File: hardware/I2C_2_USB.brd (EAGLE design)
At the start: 14.9 x 20.3 mm, 13 parts, among them CN1 1X4-BIG, J3 USB-MICROB, U1 ATMEGA328P-MU-QFN32

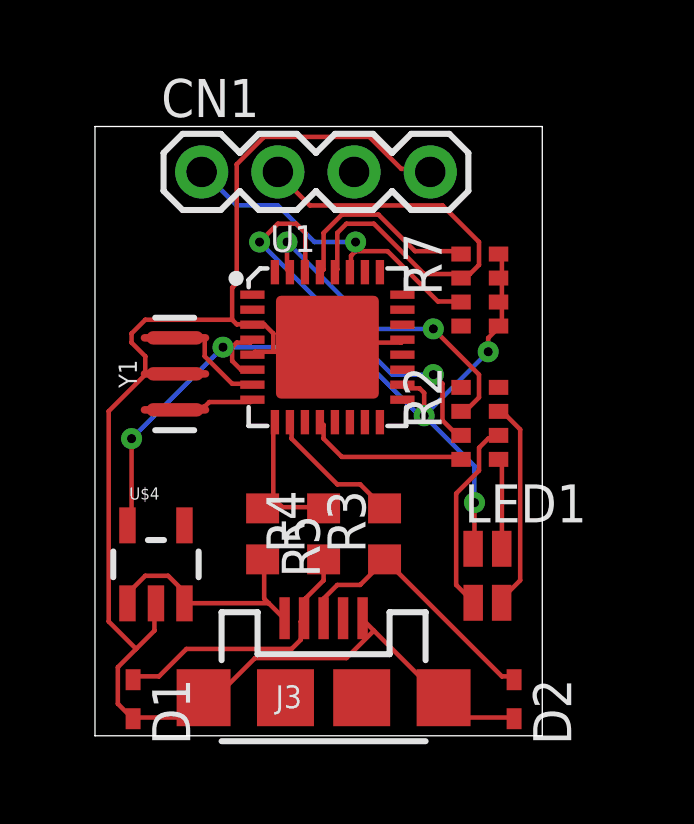
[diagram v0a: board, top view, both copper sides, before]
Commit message: Add RST pushbutton, GND planes
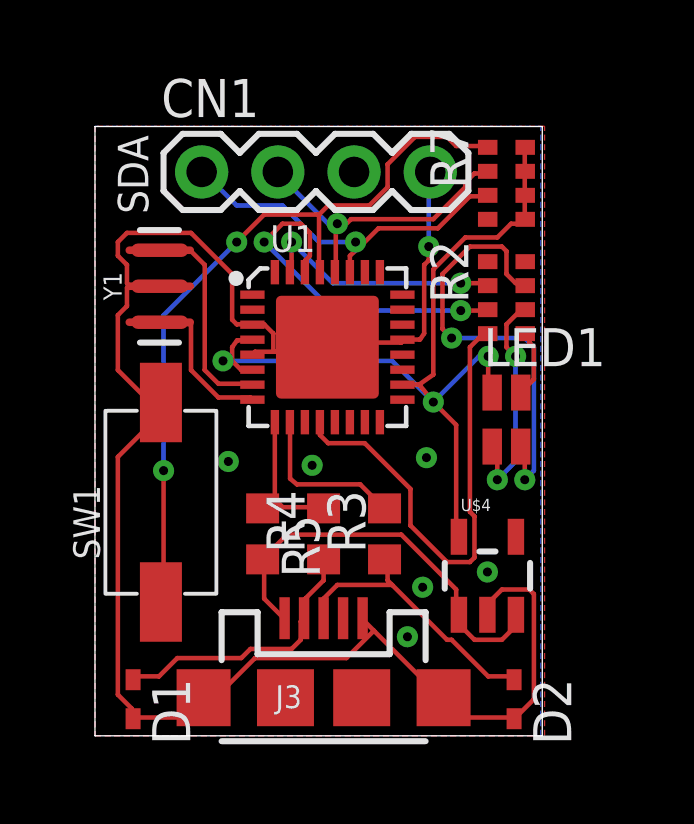
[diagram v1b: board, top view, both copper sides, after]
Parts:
- added SW1: (no value), Seeed-OPL-Switch:SW2-4.0-6.0X3.0X2.5MM
- moved U$4 11.1 mm to (13.1, 5.33)
- moved LED1 5.25 mm to (13.7, 10.5)
- moved R2 4.28 mm to (13.7, 14.6)
- moved R7 3.67 mm to (13.7, 18.4)
- moved Y1 2.96 mm to (2.16, 15.0)
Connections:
- net GND: now also SW1.2
- net RST: now also SW1.1
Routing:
- net RST: track 6.80 -> 25.7 mm, vias 0 -> 2
- net LED: track 5.52 -> 16.0 mm
- net GREEN: track 7.01 -> 15.0 mm, vias 0 -> 2
- net +5V: track 8.27 -> 13.7 mm
- net SCL: track 15.7 -> 10.2 mm, vias 0 -> 1
- net GND: track 55.5 -> 60.2 mm, vias 0 -> 7
- net XTAL1: track 3.58 -> 6.98 mm
- net TXD: track 10.8 -> 8.15 mm
- net XTAL2: track 2.69 -> 5.03 mm
- net RXD: track 13.3 -> 11.7 mm
- net BLUE: track 6.56 -> 7.57 mm, vias 0 -> 2
- net SDA: track 11.4 -> 12.3 mm
- net D+: track 4.62 -> 5.43 mm
- net RED: track 3.04 -> 2.26 mm
- net +3V3: track 30.8 -> 30.1 mm, vias 5 -> 3
- added copper zone on layer 1, net GND
- added copper zone on layer 16, net GND
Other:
- board text added: "SDA"
